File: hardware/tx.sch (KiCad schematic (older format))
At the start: 54 parts, among them Q1 RE1C002UN, U1 ADF4158, U10 HMC431LP4, U12 PAT1220-6dB, U14 MGA-25203, U15 SMA, U3 PAT1220-6dB, U7 TLV172DCK

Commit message: Current working version.
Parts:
- removed C32: 100n, fmcw3:C_0402b, symbol C
- removed C33, C34: 100p, fmcw3:C_0402b, symbol C
- removed R10: 6.98k, fmcw3:R_0402b, symbol R
- removed R14: 39k, fmcw3:R_0402b, symbol R
- removed U14: MGA-25203, fmcw3:MGA-25203, symbol MGA-25203
- added C232: 2.2u, Capacitor_SMD:C_0603_1608Metric, symbol Device:C
- added C233, C234: 100p, Capacitor_SMD:C_0402_1005Metric, symbol Device:C
- added C32, C33: DNP, Capacitor_SMD:C_0603_1608Metric, symbol Device:C
- added C34: 10u, Capacitor_SMD:C_0805_2012Metric, symbol Device:C
- added FB9: CIC21P101NE, fmcw3:C_0805b, symbol Device:Ferrite_Bead
- added U37: SE2567L, fmcw3:MGA-25203, symbol fmcw3-rescue:SE2567L
- C10, C11, C14, C176, C2, C21, C28, C29, C3, C36, C4, C40, C41, C43, C5, C6, C7, C8: footprint fmcw3:C_0402b -> Capacitor_SMD:C_0402_1005Metric; symbol C -> Device:C
- C214, C215, C26, C38: footprint fmcw3:C_0805b -> Capacitor_SMD:C_0805_2012Metric; symbol C -> Device:C
- C37, C39: footprint fmcw3:C_0603b -> Capacitor_SMD:C_0603_1608Metric; symbol C -> Device:C
- FB2, FB3, FB4: symbol FILTER -> Device:Ferrite_Bead
- Q1: symbol MOS_N_GSD -> fmcw3-rescue:MOS_N_GSD
- R1, R11, R12, R17, R18, R2, R39, R4, R40, R5, R6, R7, R9: symbol R -> Device:R
- U1: symbol ADF4158 -> fmcw3-rescue:ADF4158
- U10: symbol HMC431LP4 -> fmcw3-rescue:HMC431LP4
- U12, U3: symbol PAT1220 -> fmcw3-rescue:PAT1220
- U15: symbol SMA -> fmcw3-rescue:SMA
- U7: footprint TO_SOT_Packages_SMD:SOT-353_SC-70-5 -> Package_TO_SOT_SMD:SOT-353_SC-70-5; symbol TLV172DCK -> fmcw3-rescue:TLV172DCK
- Z1: symbol BRANCHLINE -> fmcw3-rescue:BRANCHLINE
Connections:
- net labels added: 4V5, EN
- net labels removed: 1V8, BSW
- wire segments 158 -> 212
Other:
- note added: "3.3V"
- note removed: "1.8V"

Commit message: Dropped the 3 from the end of the project name.
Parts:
- FB2, FB3: footprint fmcw3:C_0603b -> fmcw:C_0603b
- FB4, FB9: footprint fmcw3:C_0805b -> fmcw:C_0603b
- Q1: footprint fmcw3:SOT-416 -> fmcw:SOT-416; symbol fmcw3-rescue:MOS_N_GSD -> fmcw-rescue:MOS_N_GSD-fmcw3-rescue
- R1, R11, R12, R17, R18, R2, R39, R4, R40, R5, R6, R7, R9: footprint fmcw3:R_0402b -> fmcw:R_0402b
- U1: footprint fmcw3:VFQFN-24 -> fmcw:VFQFN-24; symbol fmcw3-rescue:ADF4158 -> fmcw-rescue:ADF4158-fmcw3-rescue
- U10: footprint fmcw3:VQFN-24 -> fmcw:VQFN-24; symbol fmcw3-rescue:HMC431LP4 -> fmcw-rescue:HMC431LP4-fmcw3-rescue
- U12, U3: footprint fmcw3:PAT1220 -> fmcw:PAT1220; symbol fmcw3-rescue:PAT1220 -> fmcw-rescue:PAT1220-fmcw3-rescue
- U15: footprint fmcw3:CONSMA003.062 -> fmcw:CONSMA003.062; symbol fmcw3-rescue:SMA -> fmcw-rescue:SMA-fmcw3-rescue
- U37: footprint fmcw3:MGA-25203 -> Package_DFN_QFN:QFN-16-1EP_3x3mm_P0.5mm_EP1.8x1.8mm; symbol fmcw3-rescue:SE2567L -> fmcw-rescue:SE2567L-fmcw3-rescue
- U7: symbol fmcw3-rescue:TLV172DCK -> fmcw-rescue:TLV172DCK-fmcw3-rescue
- Z1: footprint fmcw3:coupler -> fmcw:coupler; symbol fmcw3-rescue:BRANCHLINE -> fmcw-rescue:BRANCHLINE-fmcw3-rescue
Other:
- note added: "-6 dBm"
- note removed: "-7 dBm"
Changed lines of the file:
@@
 EESchema Schematic File Version 4
-LIBS:fmcw3-cache
+LIBS:fmcw-cache
 EELAYER 26 0
 EELAYER END
@@
 $EndDescr
 $Comp
-L fmcw3-rescue:HMC431LP4 U10
+L fmcw-rescue:HMC431LP4-fmcw3-rescue U10
 U 1 1 54FAAD5A
 P 9100 5700
 F 0 "U10" H 9400 5350 60  0000 C CNN
 F 1 "HMC431LP4" H 9300 6000 60  0000 C CNN
-F 2 "fmcw3:VQFN-24" H 9100 5700 60  0001 C CNN
+F 2 "fmcw:VQFN-24" H 9100 5700 60  0001 C CNN
 F 3 "http://www.analog.com/media/en/technical-documentation/data-sheets/hmc431.pdf" H 9100 5700 60  0001 C CNN
 F 4 "HMC431LP4ETR" H 9100 5700 60  0001 C CNN "manf#"
@@
 $EndComp
 $Comp
-L fmcw3-rescue:ADF4158 U1
+L fmcw-rescue:ADF4158-fmcw3-rescue U1
 U 1 1 54FAADA7
 P 1500 6150
 F 0 "U1" H 3250 5950 60  0000 C CNN
 F 1 "ADF4158" H 3300 6250 60  0000 C CNN
-F 2 "fmcw3:VFQFN-24" H 1500 6150 60  0001 C CNN
+F 2 "fmcw:VFQFN-24" H 1500 6150 60  0001 C CNN
 F 3 "http://www.analog.com/media/en/technical-documentation/data-sheets/ADF4158.pdf" H 1500 6150 60  0001 C CNN
 F 4 "ADF4158CCPZ" H 1500 6150 60  0001 C CNN "manf#"
@@
 $EndComp
 $Comp
-L fmcw3-rescue:SMA U15
+L fmcw-rescue:SMA-fmcw3-rescue U15
 U 1 1 54FAB57F
 P 15700 5000
 F 0 "U15" H 15850 5000 60  0000 C CNN
 F 1 "SMA" H 15700 5150 60  0000 C CNN
-F 2 "fmcw3:CONSMA003.062" H 15700 5000 60  0001 C CNN
+F 2 "fmcw:CONSMA003.062" H 15700 5000 60  0001 C CNN
 F 3 "" H 15700 5000 60  0000 C CNN
 F 4 "CONSMA003.062" H 15700 5000 60  0001 C CNN "manf#"
@@
 F 0 "R1" H 4320 7038 40  0000 L CNN
 F 1 "5.49k" H 4320 6962 40  0000 L CNN
-F 2 "fmcw3:R_0402b" V 4180 7000 30  0001 C CNN
+F 2 "fmcw:R_0402b" V 4180 7000 30  0001 C CNN
 F 3 "" H 4250 7000 30  0000 C CNN
 	1    4250 7000
@@
 F 0 "R2" V 4630 6150 40  0000 C CNN
 F 1 "DNP" V 4557 6151 40  0000 C CNN
-F 2 "fmcw3:R_0402b" V 4480 6150 30  0001 C CNN
+F 2 "fmcw:R_0402b" V 4480 6150 30  0001 C CNN
 F 3 "" H 4550 6150 30  0000 C CNN
 	1    4550 6150
@@
 F 0 "R4" H 5270 6638 40  0000 L CNN
 F 1 "3.1k" H 5270 6562 40  0000 L CNN
-F 2 "fmcw3:R_0402b" V 5130 6600 30  0001 C CNN
+F 2 "fmcw:R_0402b" V 5130 6600 30  0001 C CNN
 F 3 "" H 5200 6600 30  0000 C CNN
 	1    5200 6600
@@
 F 0 "R9" V 10280 5550 40  0000 C CNN
 F 1 "18" V 10207 5551 40  0000 C CNN
-F 2 "fmcw3:R_0402b" V 10130 5550 30  0001 C CNN
+F 2 "fmcw:R_0402b" V 10130 5550 30  0001 C CNN
 F 3 "" H 10200 5550 30  0000 C CNN
 	1    10200 5550
@@
 F 0 "R11" V 10630 5250 40  0000 C CNN
 F 1 "18" V 10557 5251 40  0000 C CNN
-F 2 "fmcw3:R_0402b" V 10480 5250 30  0001 C CNN
+F 2 "fmcw:R_0402b" V 10480 5250 30  0001 C CNN
 F 3 "" H 10550 5250 30  0000 C CNN
 	1    10550 5250
@@
 F 0 "R12" V 10630 5850 40  0000 C CNN
 F 1 "18" V 10557 5851 40  0000 C CNN
-F 2 "fmcw3:R_0402b" V 10480 5850 30  0001 C CNN
+F 2 "fmcw:R_0402b" V 10480 5850 30  0001 C CNN
 F 3 "" H 10550 5850 30  0000 C CNN
 	1    10550 5850
@@
 -4 dBm
 $Comp
-L fmcw3-rescue:PAT1220 U12
+L fmcw-rescue:PAT1220-fmcw3-rescue U12
 U 1 1 54FB1677
 P 11200 5000
 F 0 "U12" H 11400 4700 60  0000 C CNN
 F 1 "PAT1220-6dB" H 11250 5100 60  0000 C CNN
-F 2 "fmcw3:PAT1220" H 11200 5000 60  0001 C CNN
+F 2 "fmcw:PAT1220" H 11200 5000 60  0001 C CNN
 F 3 "" H 11200 5000 60  0000 C CNN
 	1    11200 5000
@@
 27mA
 Text Notes 11550 4900 0    60   ~ 0
--7 dBm
+-6 dBm
 Text Label 2950 4650 0    60   ~ 0
 3V3
@@
 F 0 "R7" V 7866 5900 40  0000 C CNN
 F 1 "4.7k" V 7942 5900 40  0000 C CNN
-F 2 "fmcw3:R_0402b" V 7980 5900 30  0001 C CNN
+F 2 "fmcw:R_0402b" V 7980 5900 30  0001 C CNN
 F 3 "" H 8050 5900 30  0000 C CNN
 	1    8050 5900
@@
 F 0 "R6" V 7308 6550 40  0000 C CNN
 F 1 "4.7k" V 7384 6550 40  0000 C CNN
-F 2 "fmcw3:R_0402b" V 7130 6550 30  0001 C CNN
+F 2 "fmcw:R_0402b" V 7130 6550 30  0001 C CNN
 F 3 "" H 7200 6550 30  0000 C CNN
 	1    7200 6550
@@
 F 0 "R5" H 6820 6888 40  0000 L CNN
 F 1 "4.7k" H 6820 6812 40  0000 L CNN
-F 2 "fmcw3:R_0402b" V 6680 6850 30  0001 C CNN
+F 2 "fmcw:R_0402b" V 6680 6850 30  0001 C CNN
 F 3 "" H 6750 6850 30  0000 C CNN
 	1    6750 6850
@@
 $EndComp
 $Comp
-L fmcw3-rescue:PAT1220 U3
+L fmcw-rescue:PAT1220-fmcw3-rescue U3
 U 1 1 551D3333
 P 14050 5850
 F 0 "U3" H 14250 5550 60  0000 C CNN
 F 1 "PAT1220-6dB" H 14100 5950 60  0000 C CNN
-F 2 "fmcw3:PAT1220" H 14050 5850 60  0001 C CNN
+F 2 "fmcw:PAT1220" H 14050 5850 60  0001 C CNN
 F 3 "" H 14050 5850 60  0000 C CNN
 	1    14050 5850
@@
 $EndComp
 $Comp
-L fmcw3-rescue:BRANCHLINE Z1
+L fmcw-rescue:BRANCHLINE-fmcw3-rescue Z1
 U 1 1 551D7C09
 P 14400 5150
 F 0 "Z1" H 14500 4950 60  0000 C CNN
 F 1 "15dB COUPLER" H 14450 5450 60  0000 C CNN
-F 2 "fmcw3:coupler" H 14450 5000 60  0001 C CNN
+F 2 "fmcw:coupler" H 14450 5000 60  0001 C CNN
 F 3 "" H 14450 5000 60  0000 C CNN
 	1    14400 5150
@@
 F 0 "R18" V 9530 3500 40  0000 C CNN
 F 1 "4.7k" V 9457 3501 40  0000 C CNN
-F 2 "fmcw3:R_0402b" V 9380 3500 30  0001 C CNN
+F 2 "fmcw:R_0402b" V 9380 3500 30  0001 C CNN
 F 3 "" H 9450 3500 30  0000 C CNN
 	1    9450 3500
@@
 F 0 "R17" V 14830 5450 40  0000 C CNN
 F 1 "49.9" V 14757 5451 40  0000 C CNN
-F 2 "fmcw3:R_0402b" V 14680 5450 30  0001 C CNN
+F 2 "fmcw:R_0402b" V 14680 5450 30  0001 C CNN
 F 3 "" H 14750 5450 30  0000 C CNN
 	1    14750 5450
@@
 $EndComp
 $Comp
-L fmcw3-rescue:MOS_N_GSD Q1
+L fmcw-rescue:MOS_N_GSD-fmcw3-rescue Q1
 U 1 1 55324B1D
 P 9100 4050
 F 0 "Q1" H 9277 4103 60  0000 L CNN
 F 1 "RE1C002UN" H 9277 3997 60  0000 L CNN
-F 2 "fmcw3:SOT-416" H 9100 4050 60  0001 C CNN
+F 2 "fmcw:SOT-416" H 9100 4050 60  0001 C CNN
 F 3 "" H 9100 4050 60  0000 C CNN
 	1    9100 4050
@@
 F 0 "R39" V 8930 3700 40  0000 C CNN
 F 1 "47k" V 8857 3701 40  0000 C CNN
-F 2 "fmcw3:R_0402b" V 8780 3700 30  0001 C CNN
+F 2 "fmcw:R_0402b" V 8780 3700 30  0001 C CNN
 F 3 "" H 8850 3700 30  0000 C CNN
 	1    8850 3700
@@
 F 0 "R40" V 8930 4350 40  0000 C CNN
 F 1 "DNP" V 8857 4351 40  0000 C CNN
-F 2 "fmcw3:R_0402b" V 8780 4350 30  0001 C CNN
+F 2 "fmcw:R_0402b" V 8780 4350 30  0001 C CNN
 F 3 "" H 8850 4350 30  0000 C CNN
 	1    8850 4350
@@
 F 0 "FB2" V 3700 3500 50  0000 C CNN
 F 1 "BLM18PG181SN1D" V 3600 3650 50  0000 C CNN
-F 2 "fmcw3:C_0603b" H 3750 3650 60  0001 C CNN
+F 2 "fmcw:C_0603b" H 3750 3650 60  0001 C CNN
 F 3 "" H 3750 3650 60  0000 C CNN
 	1    3750 3650
@@
 F 0 "FB4" V 11600 2950 50  0000 C CNN
 F 1 "CIC21P101NE" V 11500 3100 50  0000 C CNN
-F 2 "fmcw3:C_0805b" H 11650 3100 60  0001 C CNN
+F 2 "fmcw:C_0603b" H 11650 3100 60  0001 C CNN
 F 3 "" H 11650 3100 60  0000 C CNN
 	1    11650 3100
@@
 F 0 "FB3" V 7500 4250 50  0000 C CNN
 F 1 "BLM18PG181SN1D" V 7400 4400 50  0000 C CNN
-F 2 "fmcw3:C_0603b" H 7550 4400 60  0001 C CNN
+F 2 "fmcw:C_0603b" H 7550 4400 60  0001 C CNN
 F 3 "" H 7550 4400 60  0000 C CNN
 	1    7550 4400
@@
 PA_OFF
 $Comp
-L fmcw3-rescue:TLV172DCK U7
+L fmcw-rescue:TLV172DCK-fmcw3-rescue U7
 U 1 1 59767E0A
 P 7250 5900
@@
 $EndComp
 $Comp
-L fmcw3-rescue:SE2567L U37
+L fmcw-rescue:SE2567L-fmcw3-rescue U37
 U 1 1 5B482A8E
 P 12600 5000
 F 0 "U37" H 13300 4500 60  0000 R CNN
 F 1 "SE2567L" H 13400 5500 60  0000 R CNN
-F 2 "fmcw3:MGA-25203" H 12800 4750 60  0001 C CNN
+F 2 "Package_DFN_QFN:QFN-16-1EP_3x3mm_P0.5mm_EP1.8x1.8mm" H 12800 4750 60  0001 C CNN
 F 3 "http://www.skyworksinc.com/uploads/documents/202425A.pdf" H 12800 4750 60  0001 C CNN
 F 4 "SE2567L-R" H 13350 4600 60  0001 C CNN "manf#"
@@
 F 0 "FB9" V 13900 2950 50  0000 C CNN
 F 1 "CIC21P101NE" V 13800 3100 50  0000 C CNN
-F 2 "fmcw3:C_0805b" H 13950 3100 60  0001 C CNN
+F 2 "fmcw:C_0603b" H 13950 3100 60  0001 C CNN
 F 3 "" H 13950 3100 60  0000 C CNN
 	1    13950 3100

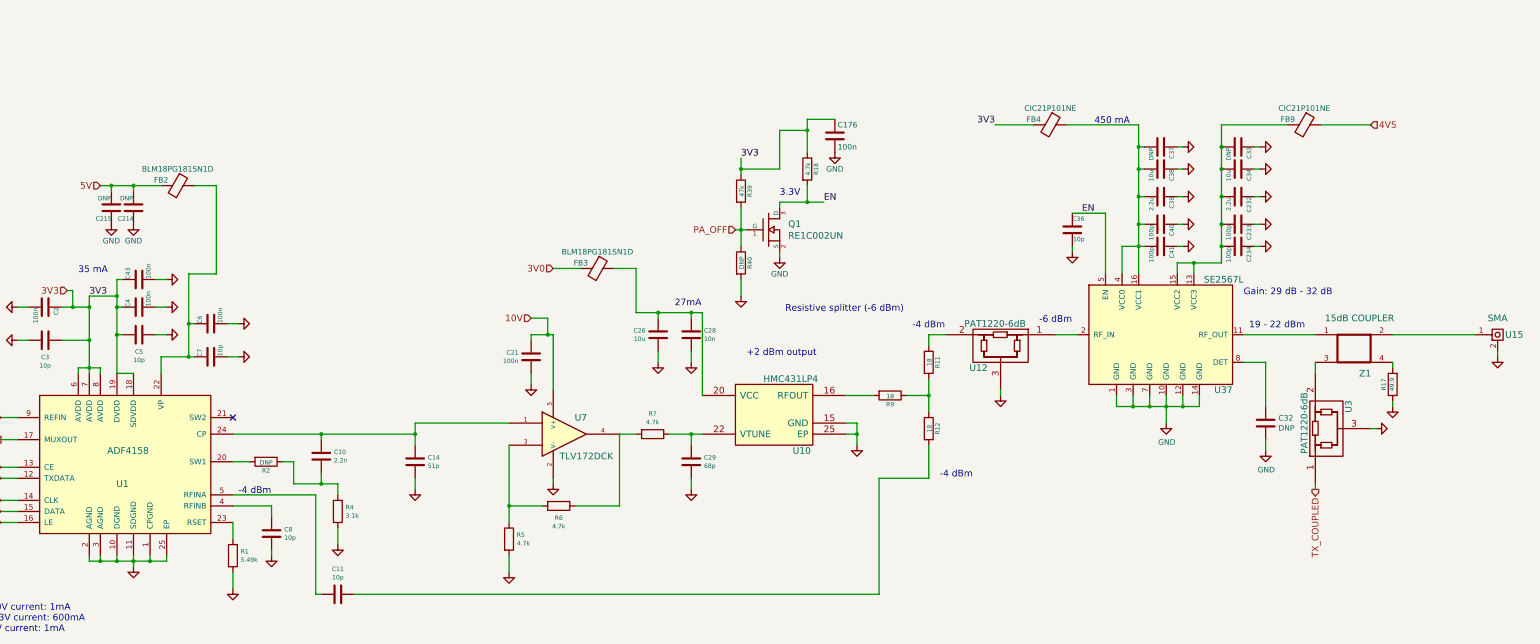
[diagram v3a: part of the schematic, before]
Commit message: Adjusted power supply for new power amplifier.
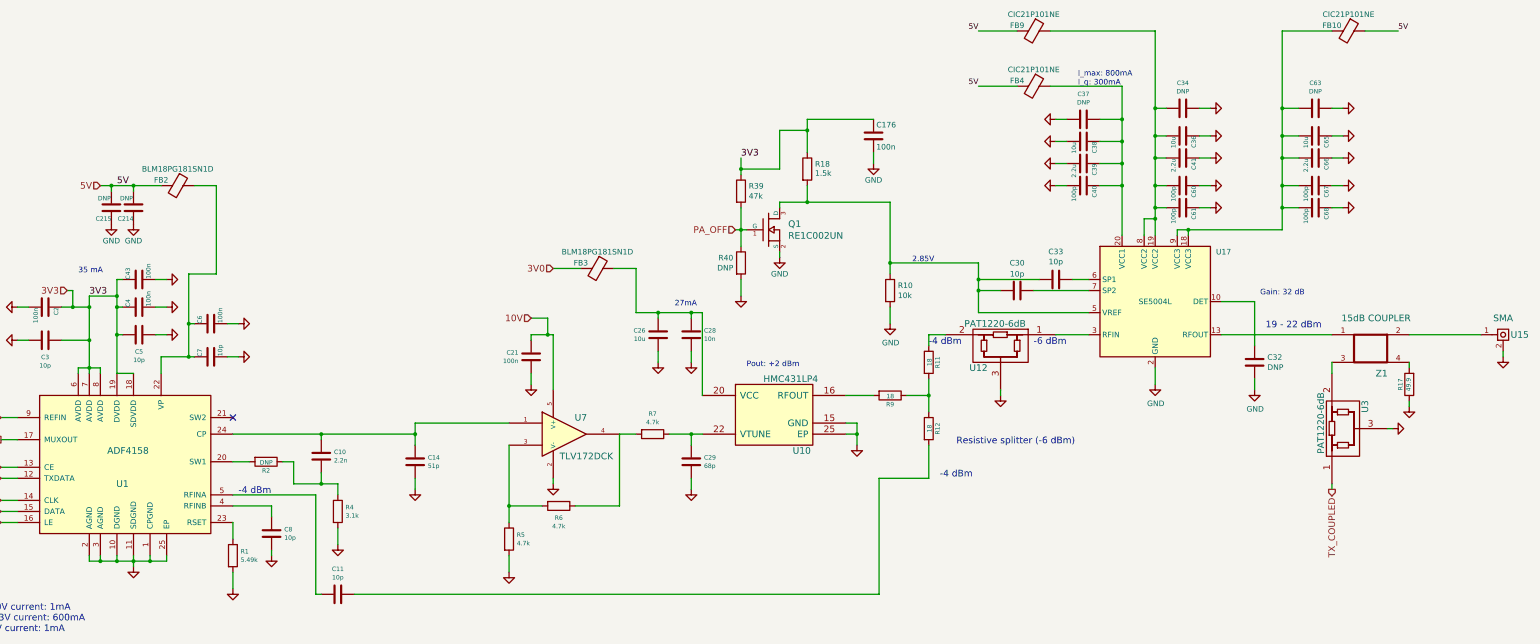
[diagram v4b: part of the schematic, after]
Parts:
- removed C232: 2.2u, Capacitor_SMD:C_0603_1608Metric, symbol Device:C
- removed C233, C234: 100p, Capacitor_SMD:C_0402_1005Metric, symbol Device:C
- removed U37: SE2567L, Package_DFN_QFN:QFN-16-1EP_3x3mm_P0.5mm_EP1.8x1.8mm, symbol fmcw-rescue:SE2567L-fmcw3-rescue
- added C30: 10p, symbol Device:C
- added C60, C61, C67, C68: 100p, Capacitor_SMD:C_0402_1005Metric, symbol Device:C
- added C63: DNP, Capacitor_SMD:C_0603_1608Metric, symbol Device:C
- added C65: 10u, Capacitor_SMD:C_0805_2012Metric, symbol Device:C
- added C66: 2.2u, Capacitor_SMD:C_0603_1608Metric, symbol Device:C
- added FB10: CIC21P101NE, fmcw:C_0603b, symbol Device:Ferrite_Bead
- added R10: 10k, symbol Device:R
- added U17: SE5004L, Package_DFN_QFN:QFN-20-1EP_4x4mm_P0.5mm_EP2.5x2.5mm, symbol RF:SE5004L
- C33: value DNP -> 10p; footprint Capacitor_SMD:C_0603_1608Metric -> (none)
- C34: value 10u -> DNP; footprint Capacitor_SMD:C_0805_2012Metric -> Capacitor_SMD:C_0603_1608Metric
- C36: value 10p -> 10u; footprint Capacitor_SMD:C_0402_1005Metric -> Capacitor_SMD:C_0805_2012Metric
- C41: value 100p -> 2.2u; footprint Capacitor_SMD:C_0402_1005Metric -> Capacitor_SMD:C_0603_1608Metric
- R18: value 4.7k -> 1.5k
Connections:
- net 3V3: no longer FB4.2
- net 5V: now also FB4.2, FB9.2, FB10.1
- net GND: now also C36.1, C37.2, C38.2, C39.2, C40.2, C60.1, C61.1, C63.1, C65.1, C66.1, C67.1, C68.1, R10.2, U17.11 (GND), U17.12 (GND), U17.14 (GND), U17.15 (GND), U17.16 (GND), U17.17 (GND), U17.2 (GND), U17.4 (GND); no longer C33.1, C36.2, C37.1, C38.1, C39.1, C40.1
- net at U12.1: now also U17.3 (RFIN)
- net at Z1.1: now also U17.13 (RFOUT)
- net at C32.1: now also U17.10 (DET)
- net 4V5: no longer names the net of FB9.1
- net 4V5: now also C34.2, C36.2, C41.2, C60.2, C61.2, U17.19 (VCC2), U17.8 (VCC2)
- net EN: no longer names the net of Q1.3 (D), R18.2
- net EN: now also C33.2, C30.2, R10.1, U17.5 (VREF); no longer C36.1
- new net: C37.1, C38.1, C39.1, C40.1, FB4.1, U17.20 (VCC1)
- new net: C63.2, C65.2, C66.2, C67.2, C68.2, FB10.2, U17.18 (VCC3), U17.9 (VCC3)
- new net: C33.1, U17.6 (SP1)
- new net: C30.1, U17.7 (SP2)
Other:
- note added: "2.85V"
- note added: "Gain: 32 dB"
- note added: "I_max: 800mA\nI_q: 300mA"
- note added: "Pout: +2 dBm"
- note removed: "+2 dBm output"
- note removed: "3.3V"
- note removed: "450 mA"
- note removed: "Gain: 29 dB - 32 dB"
- moved on the sheet: C176, C32, C37, C38, C39, C40, FB4, R17, U15, U3, Z1

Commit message: Documentation for TPS5420D buck converter.
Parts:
- C26, C36, C38, C65: MFN (none) -> 885012107014
- U1: MFN (none) -> ADF4158CCPZ; manf# ADF4158CCPZ -> (none)
- U10: MFN (none) -> HMC431LP4ETR; manf# HMC431LP4ETR -> (none)
- U15: MFN (none) -> CONSMA003.062; manf# CONSMA003.062 -> (none)
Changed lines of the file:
@@
 F 2 "fmcw:VQFN-24" H 9100 5700 60  0001 C CNN
 F 3 "http://www.analog.com/media/en/technical-documentation/data-sheets/hmc431.pdf" H 9100 5700 60  0001 C CNN
-F 4 "HMC431LP4ETR" H 9100 5700 60  0001 C CNN "manf#"
+F 4 "" H 9100 5700 60  0001 C CNN "manf#"
+F 5 "HMC431LP4ETR" H 0   0   50  0001 C CNN "MFN"
 	1    9100 5700
 	1    0    0    -1
@@
 F 2 "fmcw:VFQFN-24" H 1500 6150 60  0001 C CNN
 F 3 "http://www.analog.com/media/en/technical-documentation/data-sheets/ADF4158.pdf" H 1500 6150 60  0001 C CNN
-F 4 "ADF4158CCPZ" H 1500 6150 60  0001 C CNN "manf#"
+F 4 "" H 1500 6150 60  0001 C CNN "manf#"
+F 5 "ADF4158CCPZ" H 0   0   50  0001 C CNN "MFN"
 	1    1500 6150
 	1    0    0    -1
@@
 F 2 "fmcw:CONSMA003.062" H 15750 5000 60  0001 C CNN
 F 3 "" H 15750 5000 60  0000 C CNN
-F 4 "CONSMA003.062" H 15750 5000 60  0001 C CNN "manf#"
+F 4 "" H 15750 5000 60  0001 C CNN "manf#"
+F 5 "CONSMA003.062" H 0   0   50  0001 C CNN "MFN"
 	1    15750 5000
 	1    0    0    -1
@@
 F 2 "Capacitor_SMD:C_0805_2012Metric" H 8138 4850 30  0001 C CNN
 F 3 "" H 8100 5000 60  0000 C CNN
+F 4 "885012107014" H 0   0   50  0001 C CNN "MFN"
 	1    8100 5000
 	1    0    0    -1
@@
 F 2 "Capacitor_SMD:C_0805_2012Metric" H 11988 3100 30  0001 C CNN
 F 3 "" H 11950 3250 60  0000 C CNN
+F 4 "885012107014" H 0   0   50  0001 C CNN "MFN"
 	1    11950 3250
 	0    1    1    0
@@
 F 2 "Capacitor_SMD:C_0805_2012Metric" H 12888 3050 30  0001 C CNN
 F 3 "" H 12850 3200 60  0000 C CNN
+F 4 "885012107014" H 0   0   50  0001 C CNN "MFN"
 	1    12850 3200
 	0    1    1    0
@@
 F 2 "Capacitor_SMD:C_0805_2012Metric" H 14088 3050 30  0001 C CNN
 F 3 "" H 14050 3200 60  0000 C CNN
+F 4 "885012107014" H 0   0   50  0001 C CNN "MFN"
 	1    14050 3200
 	0    1    1    0

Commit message: Added MFNs to components.
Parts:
- C10: MFN (none) -> CL05B223KP5NNNC
- C11, C3, C5, C7, C8: MFN (none) -> GRM1555C1H100FA01D
- C14: MFN (none) -> CL05C510JB5NNNC
- C176, C2, C21, C4, C43, C6: MFN (none) -> CL05B104KO5NNNC
- C26, C36, C38, C65: MFN 885012107014 -> CL21B106KQQNNNE
- C28: MFN (none) -> GRM155R71E103KA01D
- C29: MFN (none) -> CL05C680JB5NNNC
- C30, C33: footprint (none) -> Capacitor_SMD:C_0402_1005Metric; MFN (none) -> GRM1555C1H100FA01D
- C39, C41, C66: MFN (none) -> CL10A225KO8NNNC
- C40, C60, C61, C67, C68: MFN (none) -> UMK105CG101JVHF
- FB10, FB4, FB9: footprint fmcw:C_0603b -> Inductor_SMD:L_0805_2012Metric; MFN (none) -> CIC21P101NE
- FB2, FB3: value BLM18PG181SN1D -> BLM18PG181SH1D; footprint fmcw:C_0603b -> Inductor_SMD:L_0603_1608Metric; MFN (none) -> BLM18PG181SH1D
- Q1: footprint fmcw:SOT-416 -> Package_TO_SOT_SMD:SOT-416; symbol fmcw-rescue:MOS_N_GSD-fmcw3-rescue -> Device:Q_NMOS_GSD; MFN (none) -> RE1C002UNTCL
- R1: footprint fmcw:R_0402b -> Resistor_SMD:R_0402_1005Metric; MFN (none) -> ERJ-2RKF5491X
- R10: footprint (none) -> Resistor_SMD:R_0402_1005Metric; MFN (none) -> ERJ-2RKF1002X
- R11, R12, R9: footprint fmcw:R_0402b -> Resistor_SMD:R_0402_1005Metric; MFN (none) -> ERJ-2RKF18R0X
- R17: footprint fmcw:R_0402b -> Resistor_SMD:R_0402_1005Metric; MFN (none) -> ERJ-2RKF49R9X
- R18: footprint fmcw:R_0402b -> Resistor_SMD:R_0402_1005Metric; MFN (none) -> ERJ-2RKF1501X
- R2, R40: footprint fmcw:R_0402b -> Resistor_SMD:R_0402_1005Metric
- R39: footprint fmcw:R_0402b -> Resistor_SMD:R_0402_1005Metric; MFN (none) -> ERJ-2RKF4702X
- R4: value 3.1k -> 3.09k; footprint fmcw:R_0402b -> Resistor_SMD:R_0402_1005Metric; MFN (none) -> ERJ-2RKF3091X
- R5, R6, R7: footprint fmcw:R_0402b -> Resistor_SMD:R_0402_1005Metric; MFN (none) -> ERJ-2GEJ472X
- U1: footprint fmcw:VFQFN-24 -> Package_DFN_QFN:WQFN-24-1EP_4x4mm_P0.5mm_EP2.7x2.7mm; MFN ADF4158CCPZ -> ADF4158CCPZ-RL7
- U10: footprint fmcw:VQFN-24 -> Package_DFN_QFN:VQFN-24-1EP_4x4mm_P0.5mm_EP2.45x2.45mm; MFN HMC431LP4ETR -> HMC431LP4E
- U12, U3: MFN (none) -> PAT1220-C-6DB-T5
- U15: symbol fmcw-rescue:SMA-fmcw3-rescue -> Connector:Conn_Coaxial
- U17: MFN (none) -> SE5004L-R
- U7: MFN (none) -> TLV172IDCKT
